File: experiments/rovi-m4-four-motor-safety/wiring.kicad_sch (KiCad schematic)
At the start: 8 parts, among them M1 TT motor front-left (D1 A, M1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, M2 TT motor rear-left (D1 B), M3 TT motor front-right (D2 A), M4 TT motor rear-right (D2 B), U1 ESP32-S3-N16R8 CORE board (US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, U2 TB6612FNG D1: left wheels (M1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, U3 TB6612FNG D2: right wheels

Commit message: feat(m4): one 7-wire ribbon cable per driver; schematic with drawn wires
Each driver's control header R1-R7 now takes 7 consecutive ESP32 header
pins: driver 1 L4-L10 (GPIO4-7, 15-17), driver 2 R4-R10 (GPIO1, 2, 42-38).
Each driver gets its own STBY (GPIO7, GPIO41). The schematic generator
draws every connection as a wire (lanes per channel, rails for VM, 3V3
and GND), checked against the intended netlist (25 nets, ERC 0 errors).

Co-Authored-By: Claude Opus 5.5 <noreply@anthropic.com>
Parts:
- removed BT1: 5 V power bank (motor supply; unplug = kill switc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, symbol M4:TWO_PIN
- removed M1: TT motor front-left (D1 A, M1's motor), symbol M4:TWO_PIN
- removed M2: TT motor rear-left (D1 B), symbol M4:TWO_PIN
- removed M3: TT motor front-right (D2 A), symbol M4:TWO_PIN
- removed M4: TT motor rear-right (D2 B), symbol M4:TWO_PIN
- removed U3: TB6612FNG D2: right wheels, symbol M4:TB6612FNG_BOARD
- added BT1: 5 V power bank (unplug = kill switch), symbol M4:POWER_BANK
- added M1: Motor front-left (D1 A), symbol M4:MOTOR
- added M2: Motor rear-left (D1 B), symbol M4:MOTOR
- added M3: Motor front-right (D2 A), symbol M4:MOTOR_MIRRORED
- added M4: Motor rear-right (D2 B), symbol M4:MOTOR_MIRRORED
- added U3: D2: TB6612FNG, right wheels (drawn mirrored), symbol M4:TB6612FNG_BOARD_MIRRORED
- U2: value TB6612FNG D1: left wheels (M1's driver) -> D1: TB6612FNG, left wheels
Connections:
- net 3V3: now also U3.L2 (VCC)
- net D1_AIN1: now also U1.L6 (6); no longer U1.L5 (5)
- net D1_AIN2: now also U1.L5 (5); no longer U1.L6 (6)
- net D1_AO1: now also M1.1
- net D1_AO2: now also M1.2
- net D1_BIN1: now also U1.L8 (15); no longer U1.L9 (16)
- net D1_BIN2: now also U1.L9 (16); no longer U1.L10 (17)
- net D1_BO1: now also M2.1
- net D1_BO2: now also M2.2
- net D1_PWMA: now also U1.L4 (4); no longer U1.L7 (7)
- net D1_PWMB: now also U1.L10 (17); no longer U1.L8 (15)
- net D2_AIN1: now also U1.R6 (42), U3.R3 (AIN1); no longer U1.L15 (9)
- net D2_AIN2: now also U1.R5 (2), U3.R2 (AIN2); no longer U1.L16 (10)
- net D2_AO1: now also M3.1, U3.L4 (AO1)
- net D2_AO2: now also M3.2, U3.L5 (AO2)
- net D2_BIN1: now also U1.R8 (40), U3.R5 (BIN1); no longer U1.L18 (12)
- net D2_BIN2: now also U1.R9 (39), U3.R6 (BIN2); no longer U1.L19 (13)
- net D2_BO1: now also M4.1, U3.L7 (BO1)
- net D2_BO2: now also M4.2, U3.L6 (BO2)
- net D2_PWMA: now also U1.R4 (1), U3.R1 (PWMA); no longer U1.L12 (8)
- net D2_PWMB: now also U1.R10 (38), U3.R7 (PWMB); no longer U1.L17 (11)
- net GND: now also U1.R1 (GND), BT1.2 (-), U3.L3 (GND); no longer U2.L8 (GND), U2.R8 (GND)
- net VM: now also BT1.1 (+5V), U3.L1 (VM)
- net D2_STBY: now reaches U1.R7 (41)
- net D2_STBY: now also U3.R4 (STBY)
- net STBY renamed D1_STBY
- net D1_STBY: now also U1.L7 (7); no longer U1.L4 (4)
- no-connect marks 28 -> 30
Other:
- note added: "Rovi M4 wiring: four TT motors, two TB6612FNG drivers, ESP32-S3, 5 V power bank. Same pins as WIRING.md. Ribbon cables: ESP32 left header L4-L10 (GPIO 4,5,6,7,15,16,17) -> D1 R1-R7; right header R4-R10 (GPIO 1,2,42,41,40,39,38) -> D2 R1-R7. Each driver has its own STBY (GPIO7, GPIO41), low from boot and unless armed; the TB6612 pull-down holds it low in reset. Firmware CHANNELS: D1 A=FL, D1 B=RL,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"
- note removed: "Rovi M4 wiring: four TT motors, two TB6612FNG drivers, ESP32-S3, 5 V power bank. Same pins as WIRING.md. Nets join by label name. M1's wiring is D1 channel A (GPIO4-7) and is kept; everything new is on the ESP32 left header. One STBY line (GPIO4) for both drivers: low from boot and unless armed; the TB6612 pull-down holds it low in reset. Skipped: GPIO18 (high glitch at power-up), GPIO3/46 (strap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"

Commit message: feat(m4): driver 2 ribbon on ESP32 left header L14-L20 (GPIO46, 9-14)
Both ribbons now come off the left header: driver 1 L4-L10, driver 2
L14-L20; STBY on GPIO7 and GPIO11. Schematic regenerated (25 nets match,
ERC 0 errors).

Co-Authored-By: Claude Opus 5.5 <noreply@anthropic.com>
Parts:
- M3, M4: symbol M4:MOTOR_MIRRORED -> M4:MOTOR
- U3: value D2: TB6612FNG, right wheels (drawn mirrored) -> D2: TB6612FNG, right wheels; symbol M4:TB6612FNG_BOARD_MIRRORED -> M4:TB6612FNG_BOARD
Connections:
- net D2_AIN1: now also U1.L16 (10); no longer U1.R6 (42)
- net D2_AIN2: now also U1.L15 (9); no longer U1.R5 (2)
- net D2_BIN1: now also U1.L18 (12); no longer U1.R8 (40)
- net D2_BIN2: now also U1.L19 (13); no longer U1.R9 (39)
- net D2_PWMA: now also U1.L14 (46); no longer U1.R4 (1)
- net D2_PWMB: now also U1.L20 (14); no longer U1.R10 (38)
- net D2_STBY: now also U1.L17 (11); no longer U1.R7 (41)
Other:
- note added: "Rovi M4 wiring: four TT motors, two TB6612FNG drivers, ESP32-S3, 5 V power bank. Same pins as WIRING.md. Ribbon cables: ESP32 left header L4-L10 (GPIO 4,5,6,7,15,16,17) -> D1 R1-R7; L14-L20 (GPIO 46,9,10,11,12,13,14) -> D2 R1-R7. Each driver has its own STBY (GPIO7, GPIO11), low from boot and unless armed; the TB6612 pull-down holds it low in reset. Firmware CHANNELS: D1 A=FL, D1 B=RL, D2 A=FR, D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"
- note removed: "Rovi M4 wiring: four TT motors, two TB6612FNG drivers, ESP32-S3, 5 V power bank. Same pins as WIRING.md. Ribbon cables: ESP32 left header L4-L10 (GPIO 4,5,6,7,15,16,17) -> D1 R1-R7; right header R4-R10 (GPIO 1,2,42,41,40,39,38) -> D2 R1-R7. Each driver has its own STBY (GPIO7, GPIO41), low from boot and unless armed; the TB6612 pull-down holds it low in reset. Firmware CHANNELS: D1 A=FL, D1 B=RL,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"
- moved on the sheet: BT1, M1, M2, M3, M4, U3

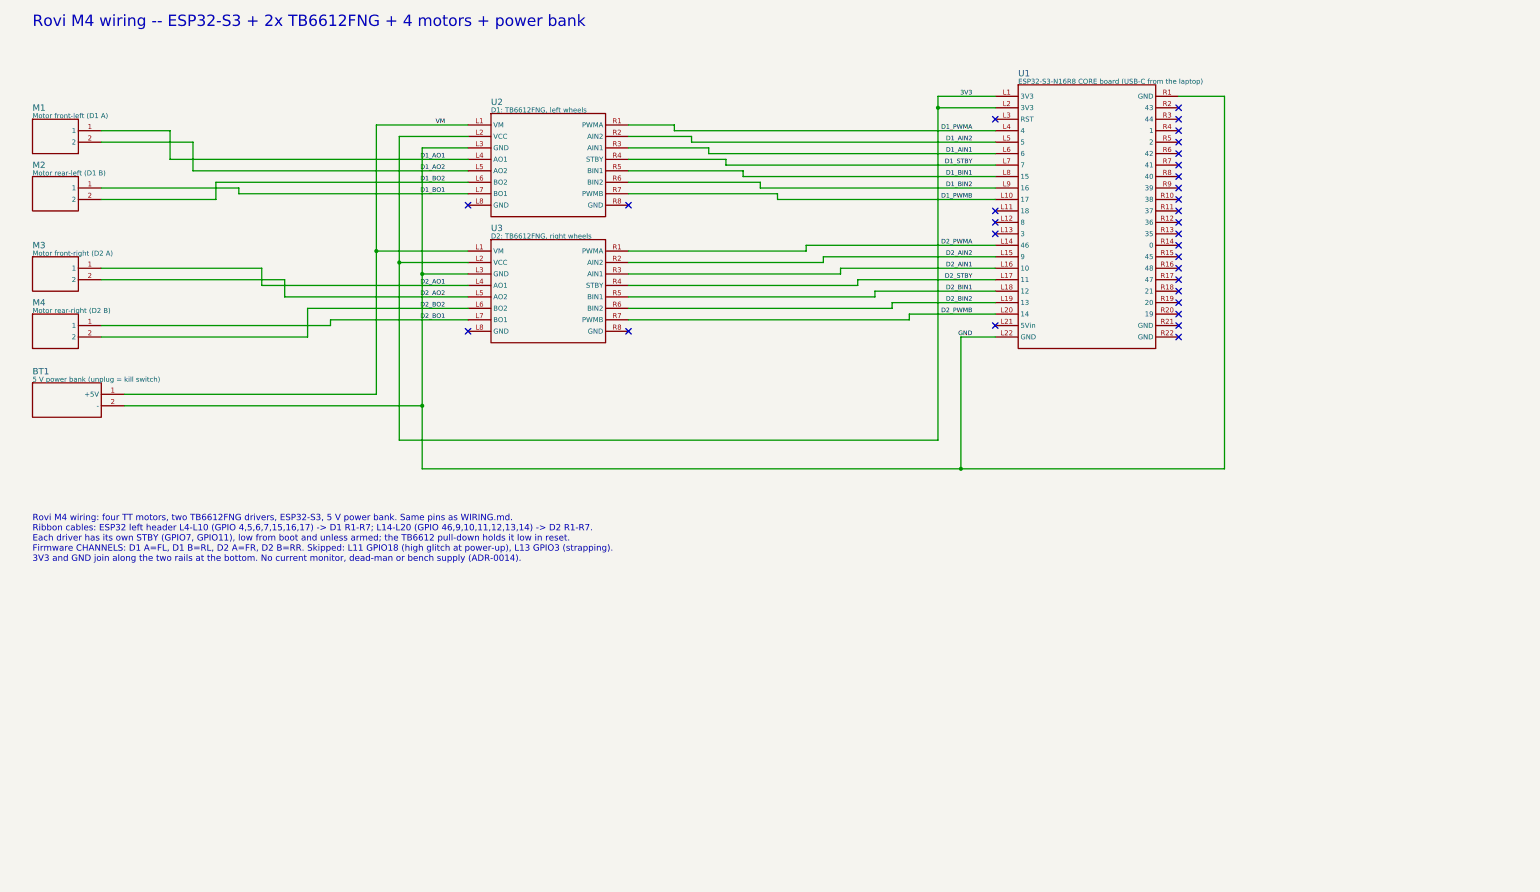
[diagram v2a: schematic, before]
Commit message: docs(m4): two power banks (motors, ESP32) and decoupling capacitors in the wiring and schematic
BT1 feeds both drivers' VM; BT2 feeds the ESP32 through its USB-C port.
C1/C2 220-470 uF at each driver's VM, C3-C6 100 nF across each motor.
Schematic regenerated: 26 nets match, ERC 0 errors.

Co-Authored-By: Claude Opus 5.5 <noreply@anthropic.com>
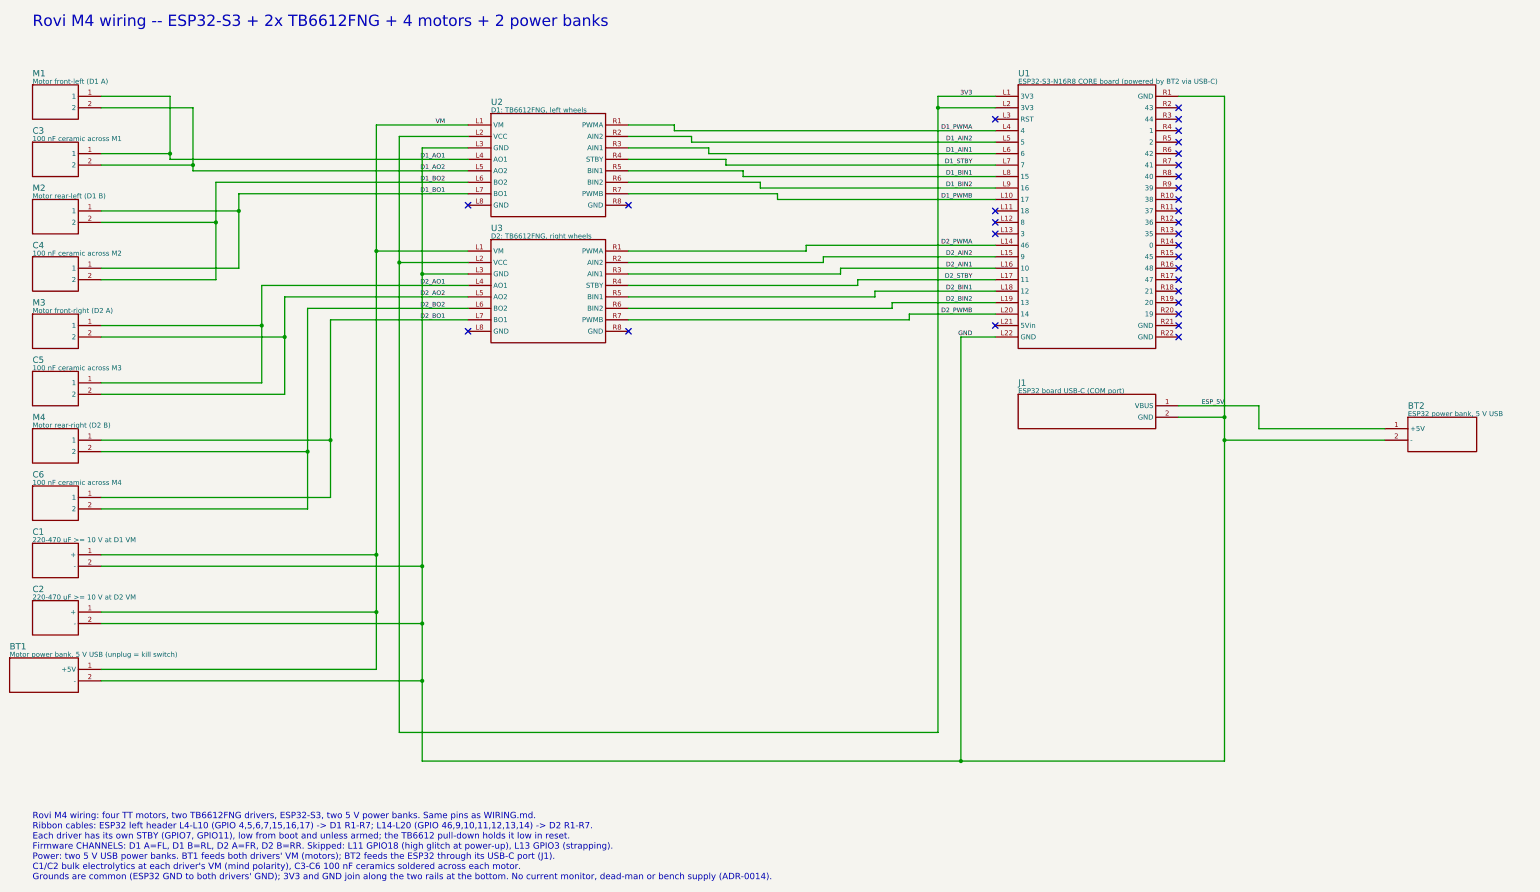
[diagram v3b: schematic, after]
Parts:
- added BT2: ESP32 power bank, 5 V USB, symbol M4:POWER_BANK_MIRRORED
- added C1: 220-470 uF >= 10 V at D1 VM, symbol M4:CAP_POLARIZED
- added C2: 220-470 uF >= 10 V at D2 VM, symbol M4:CAP_POLARIZED
- added C3: 100 nF ceramic across M1, symbol M4:CAP
- added C4: 100 nF ceramic across M2, symbol M4:CAP
- added C5: 100 nF ceramic across M3, symbol M4:CAP
- added C6: 100 nF ceramic across M4, symbol M4:CAP
- added J1: ESP32 board USB-C (COM port), symbol M4:USB_C_ON_BOARD
- BT1: value 5 V power bank (unplug = kill switch) -> Motor power bank, 5 V USB (unplug = kill switch)
- U1: value ESP32-S3-N16R8 CORE board (USB-C from the laptop) -> ESP32-S3-N16R8 CORE board (powered by BT2 via USB-C)
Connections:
- net D1_AO1: now also C3.1
- net D1_AO2: now also C3.2
- net D1_BO1: now also C4.1
- net D1_BO2: now also C4.2
- net D2_AO1: now also C5.1
- net D2_AO2: now also C5.2
- net D2_BO1: now also C6.1
- net D2_BO2: now also C6.2
- net GND: now also BT2.2 (-), C1.2 (-), C2.2 (-), J1.2 (GND)
- net VM: now also C1.1 (+), C2.1 (+)
- new net ESP_5V: BT2.1 (+5V), J1.1 (VBUS)
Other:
- note added: "Rovi M4 wiring -- ESP32-S3 + 2x TB6612FNG + 4 motors + 2 power banks"
- note added: "Rovi M4 wiring: four TT motors, two TB6612FNG drivers, ESP32-S3, two 5 V power banks. Same pins as WIRING.md. Ribbon cables: ESP32 left header L4-L10 (GPIO 4,5,6,7,15,16,17) -> D1 R1-R7; L14-L20 (GPIO 46,9,10,11,12,13,14) -> D2 R1-R7. Each driver has its own STBY (GPIO7, GPIO11), low from boot and unless armed; the TB6612 pull-down holds it low in reset. Firmware CHANNELS: D1 A=FL, D1 B=RL, D2 A=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"
- note removed: "Rovi M4 wiring -- ESP32-S3 + 2x TB6612FNG + 4 motors + power bank"
- note removed: "Rovi M4 wiring: four TT motors, two TB6612FNG drivers, ESP32-S3, 5 V power bank. Same pins as WIRING.md. Ribbon cables: ESP32 left header L4-L10 (GPIO 4,5,6,7,15,16,17) -> D1 R1-R7; L14-L20 (GPIO 46,9,10,11,12,13,14) -> D2 R1-R7. Each driver has its own STBY (GPIO7, GPIO11), low from boot and unless armed; the TB6612 pull-down holds it low in reset. Firmware CHANNELS: D1 A=FL, D1 B=RL, D2 A=FR, D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"
- moved on the sheet: BT1, M1, M2, M3, M4
